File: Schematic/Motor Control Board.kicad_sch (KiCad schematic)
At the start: 0 parts

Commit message: 1st Schematic Review
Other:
- added sheet Quadrature Counter (Quadrature Counter.kicad_sch)
- sheet Motor Drivers ports: added MOTORx_nFAULT, SPI_SCLK, SPI_SDI, SPI_SDO; removed MOTOR1_nFAULT, MOTOR2_nFAULT, MOTOR3_nFAULT, MOTOR4_nFAULT, MOTORx_SCLK, MOTORx_SDI, MOTORx_SDO

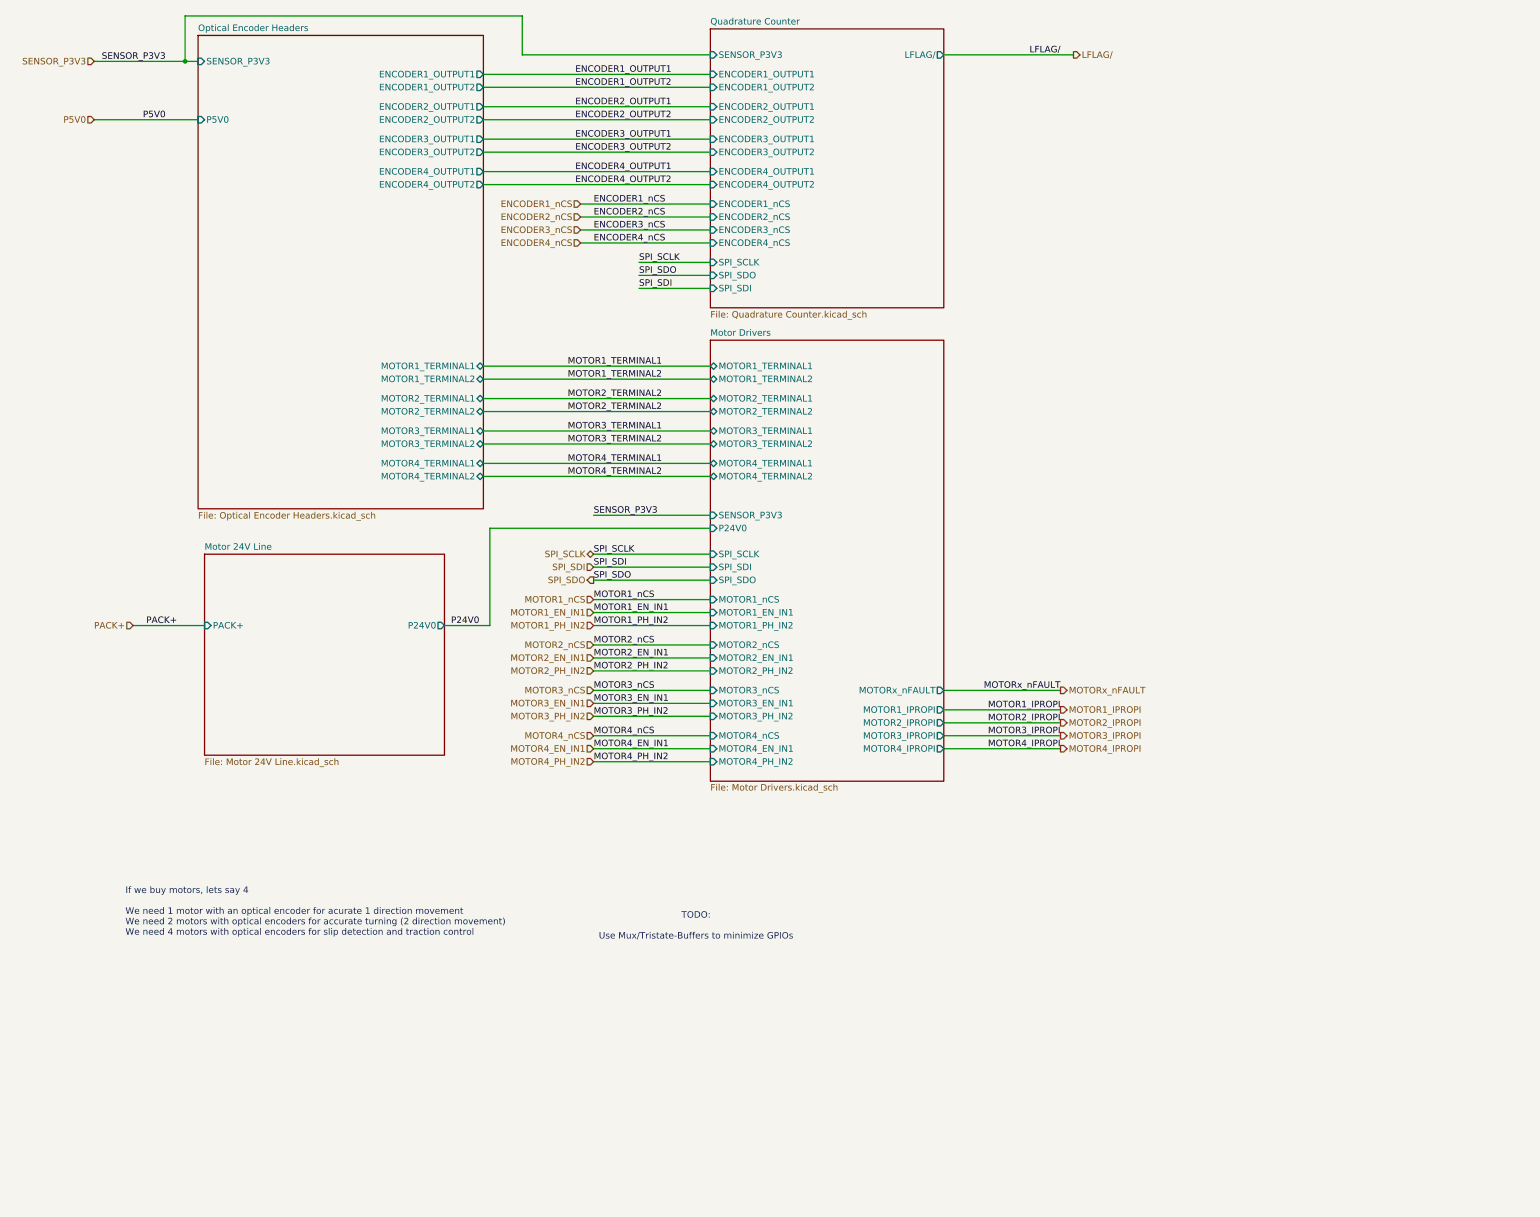
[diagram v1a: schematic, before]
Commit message: Added MCU
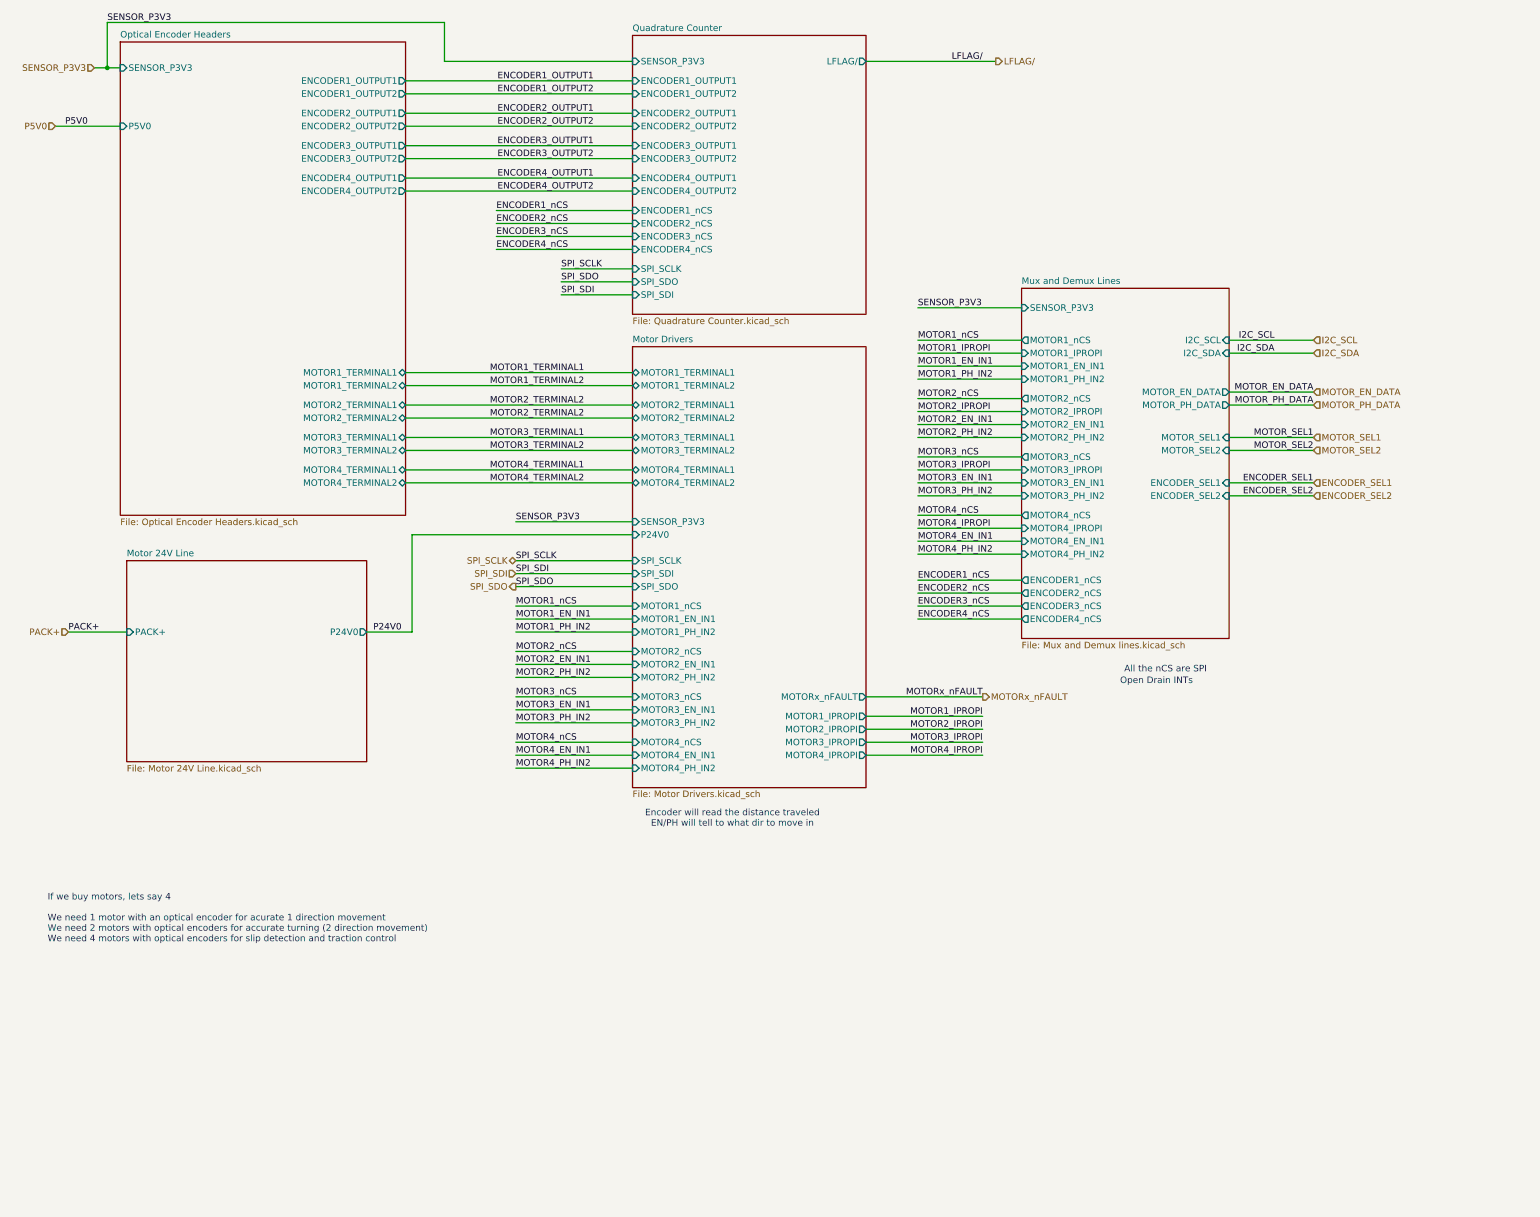
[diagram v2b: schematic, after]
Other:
- added sheet Mux and Demux Lines (Mux and Demux lines.kicad_sch)
- note added: "All the nCS are SPI"
- note added: "Encoder will read the distance traveled EN/PH will tell to what dir to move in"
- note added: "Open Drain INTs"
- note removed: "TODO: Use Mux/Tristate-Buffers to minimize GPIOs"

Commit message: Massive pivit, simplification
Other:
- removed sheet Motor 24V Line
- removed sheet Mux and Demux Lines
- added sheet Motor 6V Line (Motor 6V Line.kicad_sch)
- sheet Motor Drivers ports: added MCU_P3V3, MOTOR1_nFAULT, MOTOR2_nFAULT, P6V0; removed MOTOR3_EN_IN1, MOTOR3_IPROPI, MOTOR3_PH_IN2, MOTOR3_TERMINAL1, MOTOR3_TERMINAL2, MOTOR3_nCS, MOTOR4_EN_IN1, MOTOR4_IPROPI, MOTOR4_PH_IN2, MOTOR4_TERMINAL1, MOTOR4_TERMINAL2, MOTOR4_nCS, MOTORx_nFAULT, P24V0, SENSOR_P3V3
- sheet Optical Encoder Headers ports: added MCU_P3V3; removed ENCODER3_OUTPUT1, ENCODER3_OUTPUT2, ENCODER4_OUTPUT1, ENCODER4_OUTPUT2, MOTOR3_TERMINAL1, MOTOR3_TERMINAL2, MOTOR4_TERMINAL1, MOTOR4_TERMINAL2, SENSOR_P3V3
- sheet Quadrature Counter ports: added ENCODER1_LFLAG/, ENCODER2_LFLAG/, MCU_P3V3; removed ENCODER3_OUTPUT1, ENCODER3_OUTPUT2, ENCODER3_nCS, ENCODER4_OUTPUT1, ENCODER4_OUTPUT2, ENCODER4_nCS, LFLAG/, SENSOR_P3V3
- note removed: "All the nCS are SPI"
- note removed: "Encoder will read the distance traveled EN/PH will tell to what dir to move in"
- note removed: "If we buy motors, lets say 4 We need 1 motor with an optical encoder for acurate 1 direction movement We need 2 motors with optical encoders for accurate turning (2 direction movement) We need 4 motors with optical encoders for slip detection and traction control"
- note removed: "Open Drain INTs"

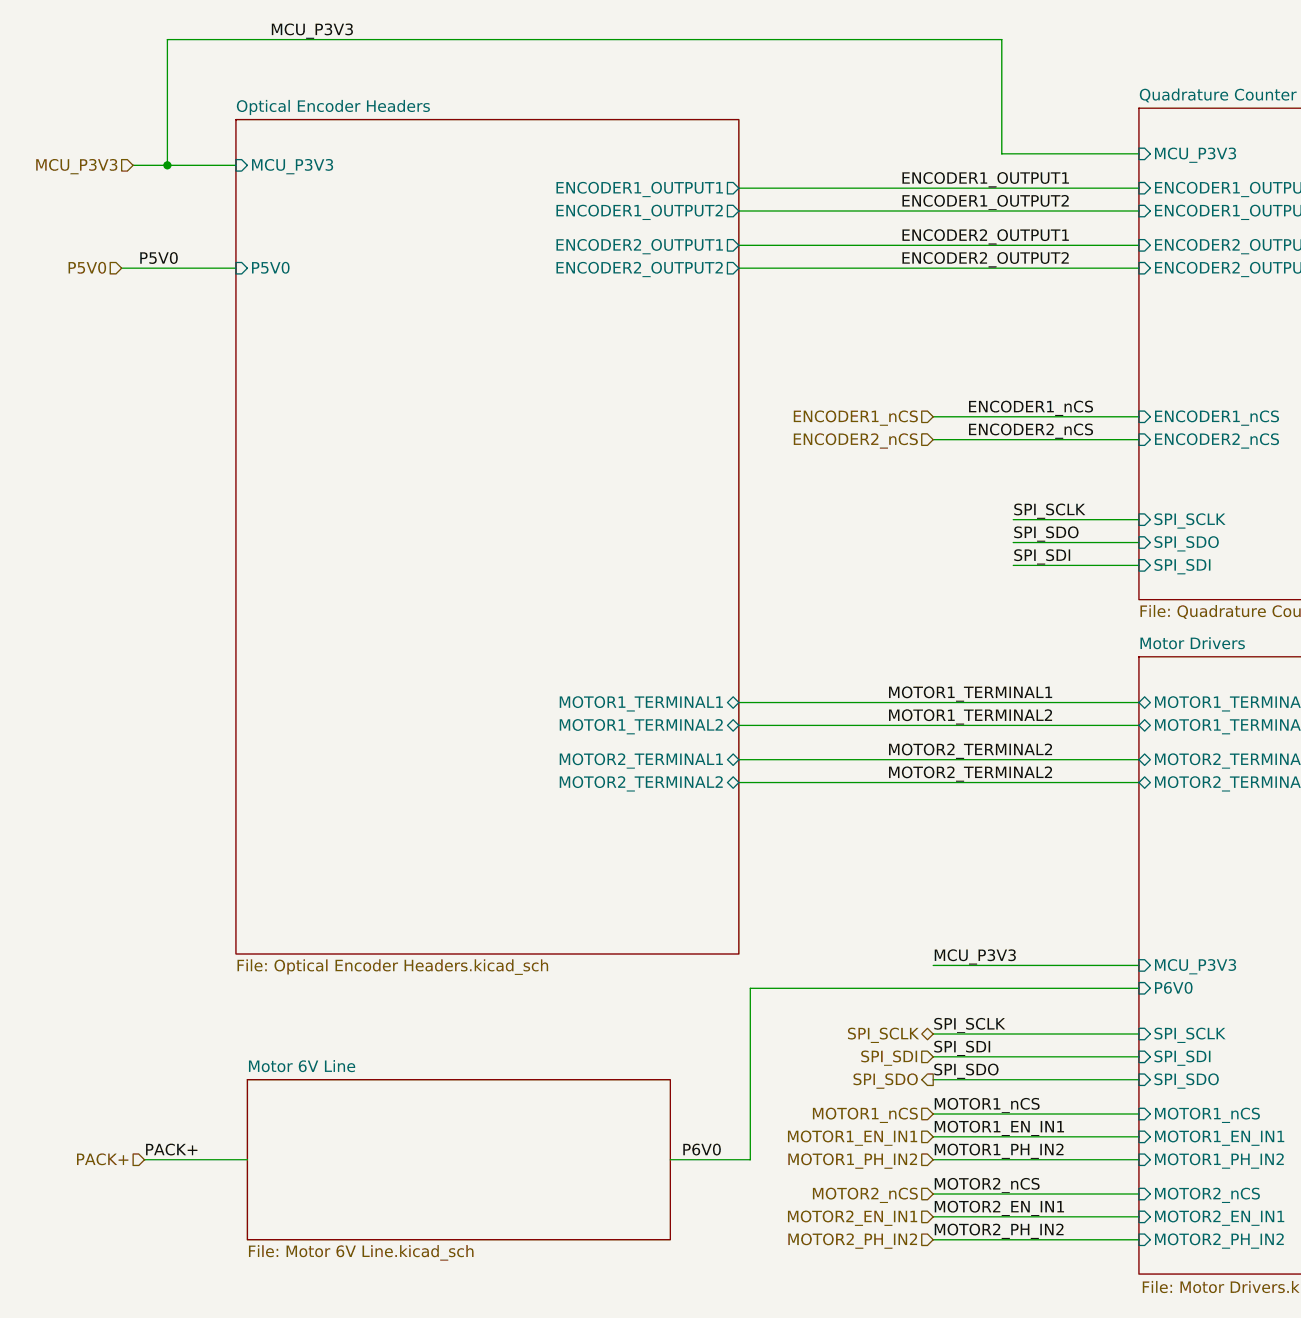
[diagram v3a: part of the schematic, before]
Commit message: now need 6V Line
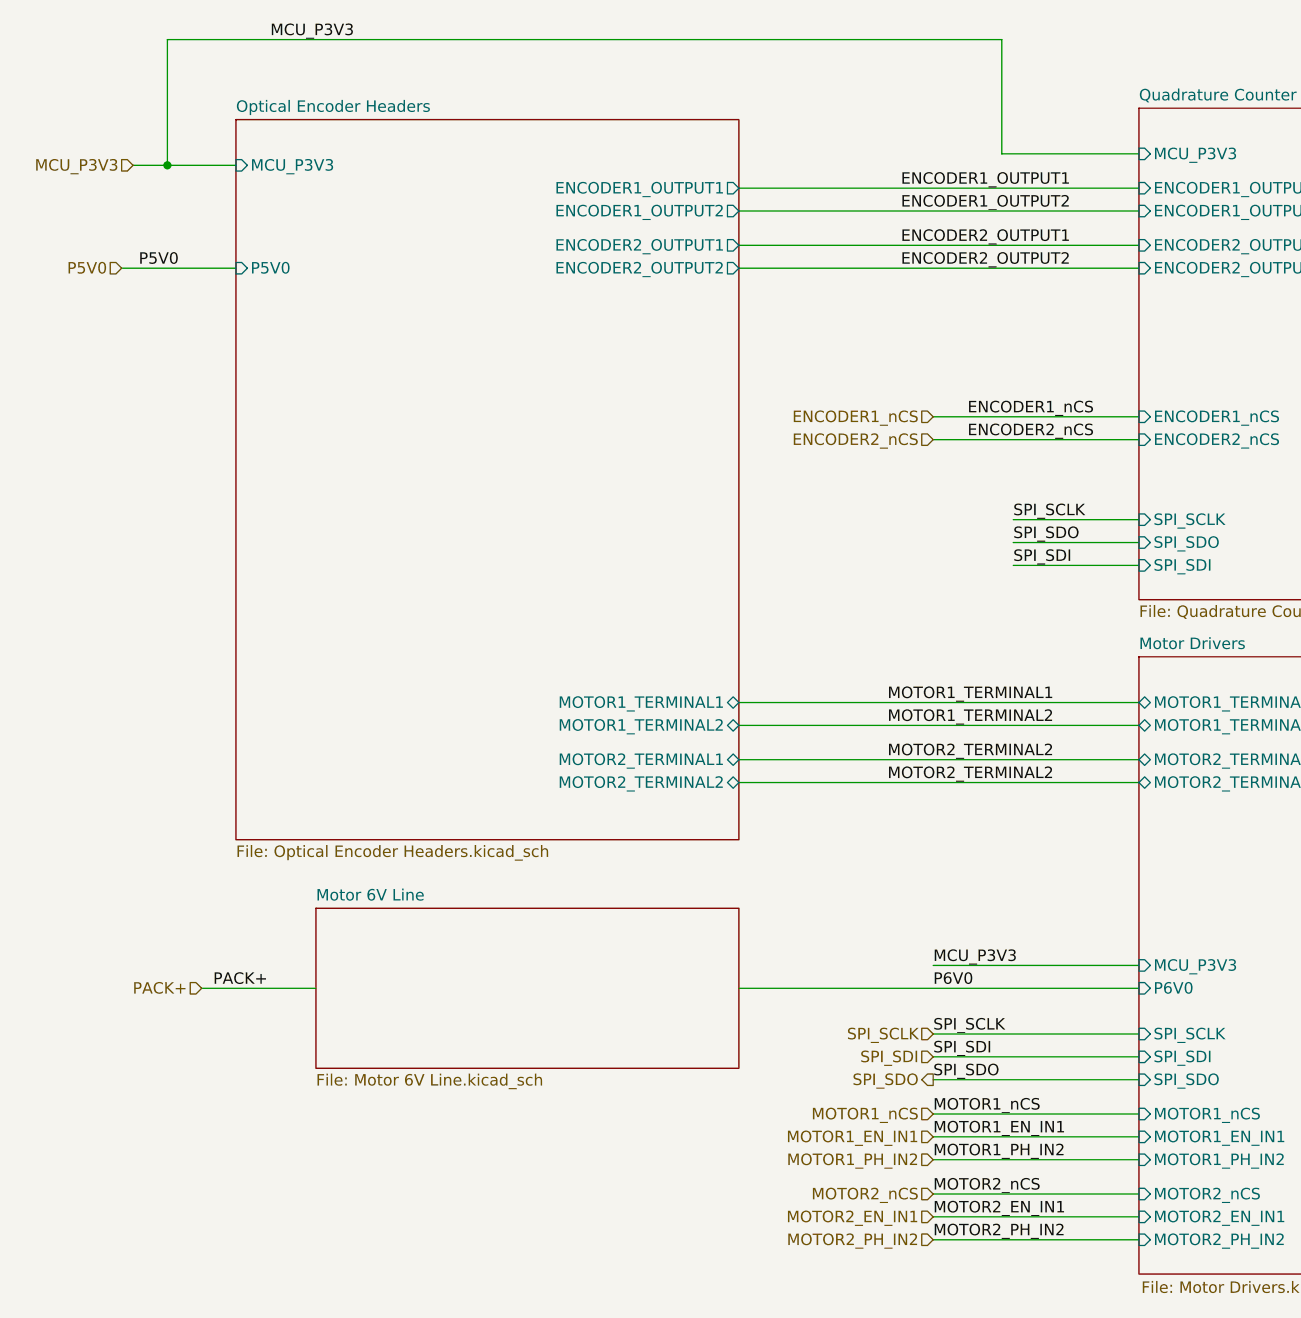
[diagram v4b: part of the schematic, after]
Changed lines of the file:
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@@
-	(wire
-		(pts
-			(xy 128.27 130.81) (xy 171.45 130.81)
-		)
-		(stroke
-			(width 0)
-			(type default)
-		)
-	)
 	(wire
 		(pts
@@
 	(wire
 		(pts
-			(xy 128.27 130.81) (xy 128.27 149.86)
-		)
-		(stroke
-			(width 0)
-			(type default)
-		)
-	)
-	(wire
-		(pts
 			(xy 157.48 83.82) (xy 171.45 83.82)
 		)
@@
 	(wire
 		(pts
+			(xy 67.31 130.81) (xy 80.01 130.81)
+		)
+		(stroke
+			(width 0)
+			(type default)
+		)
+	)
+	(wire
+		(pts
 			(xy 127 48.26) (xy 171.45 48.26)
 		)
@@
 	(wire
 		(pts
-			(xy 128.27 149.86) (xy 119.38 149.86)
+			(xy 127 130.81) (xy 171.45 130.81)
 		)
 		(stroke
@@
 		(pts
 			(xy 59.69 39.37) (xy 63.5 39.37)
-		)
-		(stroke
-			(width 0)
-			(type default)
-		)
-	)
-	(wire
-		(pts
-			(xy 60.96 149.86) (xy 72.39 149.86)
 		)
 		(stroke
@@
 		)
 	)
+	(label "P6V0"
+		(at 148.59 130.81 0)
+		(effects
+			(font
+				(size 1.27 1.27)
+			)
+			(justify left bottom)
+		)
+	)
 	(label "SPI_SDO"
 		(at 148.59 140.97 0)
@@
 		)
 	)
-	(label "P6V0"
-		(at 120.65 149.86 0)
-		(effects
-			(font
-				(size 1.27 1.27)
-			)
-			(justify left bottom)
-		)
-	)
 	(label "MOTOR2_TERMINAL2"
 		(at 143.51 105.41 0)
@@
 	)
 	(label "PACK+"
-		(at 60.96 149.86 0)
+		(at 68.58 130.81 0)
 		(effects
 			(font
@@
 	(hierarchical_label "PACK+"
 		(shape input)
-		(at 60.96 149.86 180)
+		(at 67.31 130.81 180)
 		(effects
 			(font
@@
 	)
 	(hierarchical_label "SPI_SCLK"
-		(shape bidirectional)
+		(shape input)
 		(at 148.59 135.89 180)
 		(effects
@@
 	(sheet
 		(at 71.12 34.29)
-		(size 55.88 92.71)
+		(size 55.88 80.01)
 		(exclude_from_sim no)
 		(in_bom yes)
@@
 		)
 		(property "Sheetfile" "Optical Encoder Headers.kicad_sch"
-			(at 71.12 127.5846 0)
+			(at 71.12 114.8846 0)
 			(effects
 				(font
@@
 	)
 	(sheet
-		(at 72.39 140.97)
+		(at 80.01 121.92)
 		(size 46.99 17.78)
 		(exclude_from_sim no)
@@
 		)
 		(property "Sheetname" "Motor 6V Line"
-			(at 72.39 140.2584 0)
+			(at 80.01 121.2084 0)
 			(effects
 				(font
@@
 		)
 		(property "Sheetfile" "Motor 6V Line.kicad_sch"
-			(at 72.39 159.3346 0)
-			(effects
-				(font
+			(at 80.01 140.2846 0)
+			(effects
+				(font

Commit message: updated
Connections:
- no-connect marks 0 -> 4
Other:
- removed sheet Quadrature Counter
- sheet Motor 6V Line ports: added P6V0, PACK+; removed none
- sheet Motor Drivers ports: added MOTOR3_EN_IN1, MOTOR3_IPROPI, MOTOR3_PH_IN2, MOTOR3_TERMINAL1, MOTOR3_TERMINAL2, MOTOR3_nCS, MOTOR3_nFAULT, MOTOR4_EN_IN1, MOTOR4_IPROPI, MOTOR4_PH_IN2, MOTOR4_TERMINAL1, MOTOR4_TERMINAL2, MOTOR4_nCS, MOTOR4_nFAULT, P3V3; removed MCU_P3V3
- sheet Optical Encoder Headers ports: added ENCODER3_OUTPUT1, ENCODER3_OUTPUT2, ENCODER4_OUTPUT1, ENCODER4_OUTPUT2, MOTOR3_TERMINAL1, MOTOR3_TERMINAL2, MOTOR4_TERMINAL1, MOTOR4_TERMINAL2, P3V3; removed MCU_P3V3
- note added: "* We do not need 4 We can use 2"

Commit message: current
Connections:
- no-connect marks 4 -> 0
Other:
- sheet Optical Encoder Headers ports: added none; removed ENCODER3_OUTPUT1, ENCODER3_OUTPUT2, ENCODER4_OUTPUT1, ENCODER4_OUTPUT2
- note removed: "* We do not need 4 We can use 2"
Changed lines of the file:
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@@
 	(generator_version "9.0")
 	(paper "A3")
-	(text "* We do not need 4\nWe can use 2"
-		(exclude_from_sim no)
-		(at 196.85 92.456 0)
-		(effects
-			(font
-				(size 1.27 1.27)
-			)
-		)
-	)
-	(no_connect
-		(at 179.07 91.44)
-	)
-	(no_connect
-		(at 179.07 97.79)
-	)
-	(no_connect
-		(at 179.07 88.9)
-	)
-	(no_connect
-		(at 179.07 95.25)
-	)
 	(wire
 		(pts
@@
 			(effects
 				(font
-					(size 1.27 1.27)
-				)
-				(justify right)
-			)
-		)
-		(pin "ENCODER3_OUTPUT1" output
-			(at 179.07 88.9 0)
-			(effects
-				(font
-					(size 1.27 1.27)
-				)
-				(justify right)
-			)
-		)
-		(pin "ENCODER4_OUTPUT1" output
-			(at 179.07 95.25 0)
-			(effects
-				(font
-					(size 1.27 1.27)
-				)
-				(justify right)
-			)
-		)
-		(pin "ENCODER3_OUTPUT2" output
-			(at 179.07 91.44 0)
-			(effects
-				(font
-					(size 1.27 1.27)
-				)
-				(justify right)
-			)
-		)
-		(pin "ENCODER4_OUTPUT2" output
-			(at 179.07 97.79 0)
-			(effects
-				(font

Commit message: updated schematic
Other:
- sheet Motor Drivers ports: added SPI_CIPO, SPI_COPI; removed SPI_SDI, SPI_SDO
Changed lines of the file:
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@@
 		)
 	)
-	(label "SPI_SDO"
+	(label "SPI_COPI"
 		(at 200.66 190.5 0)
 		(effects
@@
 		)
 	)
-	(label "SPI_SDI"
+	(label "SPI_CIPO"
 		(at 200.66 187.96 0)
 		(effects
@@
 		)
 	)
-	(hierarchical_label "SPI_SDI"
+	(hierarchical_label "SPI_CIPO"
 		(shape input)
 		(at 200.66 187.96 180)
@@
 		)
 	)
-	(hierarchical_label "SPI_SDO"
+	(hierarchical_label "SPI_COPI"
 		(shape output)
 		(at 200.66 190.5 180)
@@
 			)
 		)
-		(pin "SPI_SDI" input
+		(pin "SPI_CIPO" input
 			(at 223.52 187.96 180)
 			(effects
@@
 			)
 		)
-		(pin "SPI_SDO" output
+		(pin "SPI_COPI" output
 			(at 223.52 190.5 180)
 			(effects
